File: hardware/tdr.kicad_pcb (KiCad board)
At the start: 4 copper layers, 98.8 x 47 mm, 238 parts, among them J201 Conn_02x01, J202 Conn_Coaxial, J203 Conn_Coaxial, J204 Conn_Coaxial, J205 Conn_Coaxial, J207 Conn_Coaxial, J208 Conn_Coaxial, J209 Conn_Coaxial, J210 Barrel_Jack_Switch, J801 Conn_02x06_Counter_Clockwise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

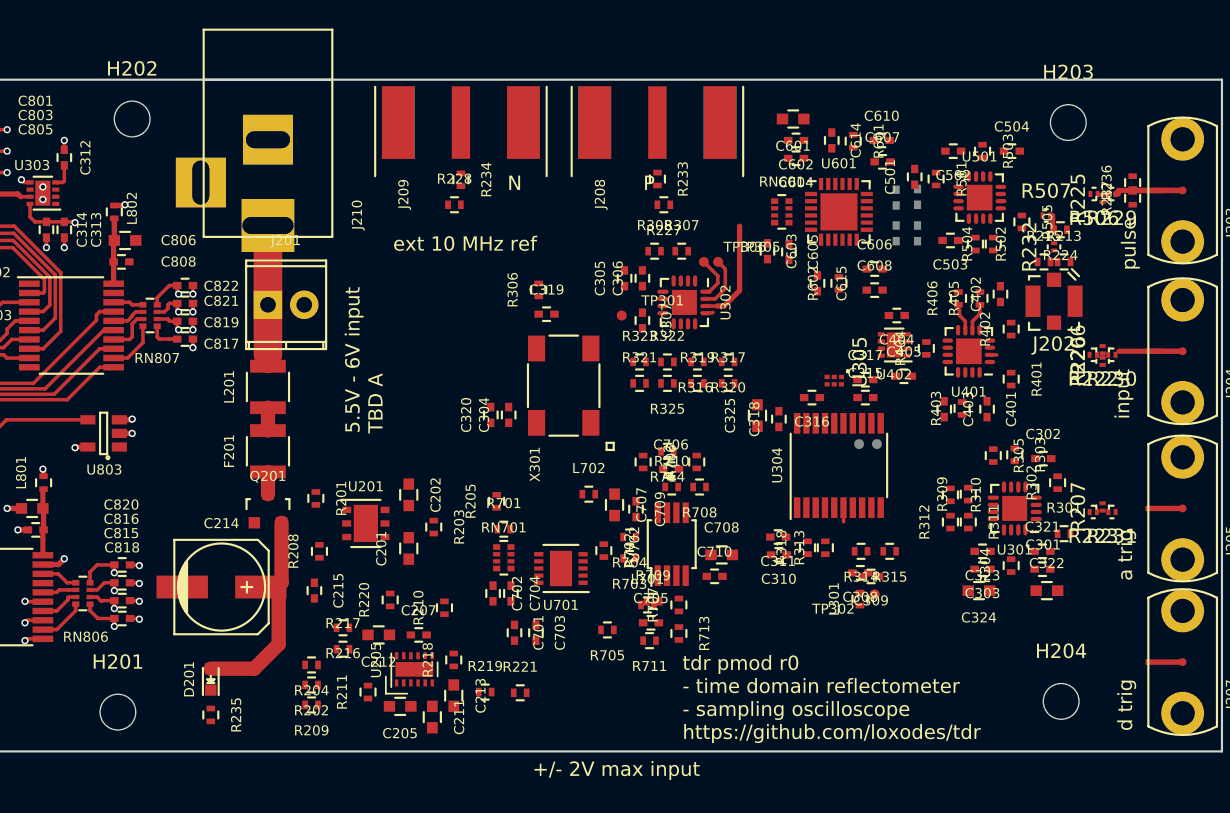
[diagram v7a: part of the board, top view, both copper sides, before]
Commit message: layout of low speed analog and power sections
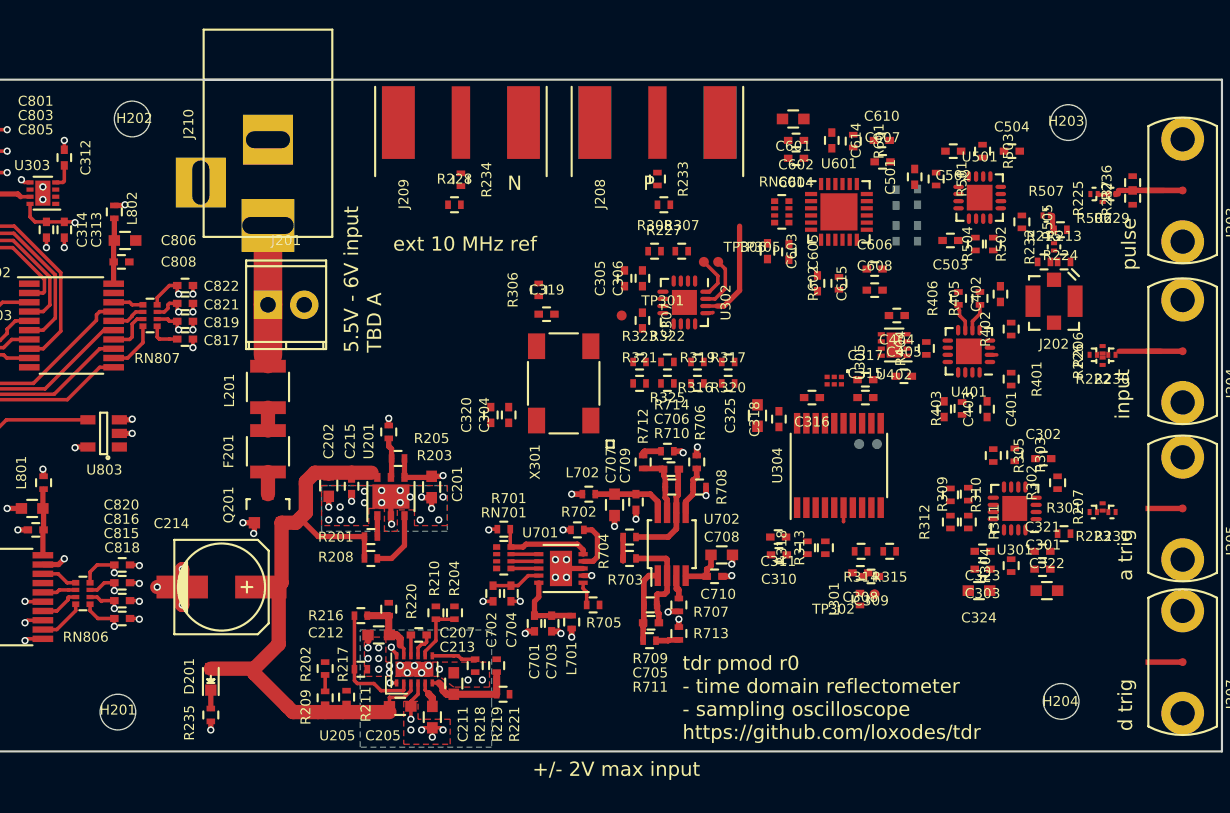
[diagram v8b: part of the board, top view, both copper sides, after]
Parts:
- moved R204 10.6 mm to (135.8, 95.8), turned to 90 degrees
- moved R205 8.97 mm to (131.2, 83.2), turned to 270 degrees
- moved C215 7.75 mm to (128.6, 87.0)
- moved C202 5.64 mm to (127.0, 86.9), turned to 90 degrees
- moved L701 5.43 mm to (144.0, 96.5), turned to 90 degrees
- moved R203 5.41 mm to (131.8, 85.0), turned to 0 degrees
- moved R201 4.69 mm to (130.0, 90.5), turned to 0 degrees
- moved C201 4.59 mm to (134.2, 87.0)
- moved R208 3.63 mm to (129.9, 92.0), turned to 0 degrees
- moved U201 2.57 mm to (131.4, 87.7), turned to 90 degrees
- moved R702 2.35 mm to (144.4, 90.0), turned to 0 degrees
- moved R705 2.02 mm to (145.5, 95.2)
- moved R219 2.02 mm to (138.8, 99.5), turned to 270 degrees
- moved R217 1.88 mm to (129.2, 99.8)
- moved R218 1.55 mm to (137.2, 99.5)
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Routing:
- net VPP: track 15.2 -> 47.6 mm
- net GND: track 22.9 -> 52.1 mm, vias 30 -> 94
- net Net-(R216-Pad2): track 0.00 -> 8.81 mm
- net Net-(C706-Pad2): track 0.00 -> 7.31 mm
- net Net-(C705-Pad2): track 0.00 -> 7.29 mm
- net Net-(R701-Pad2): track 0.00 -> 6.87 mm
- net Net-(C213-Pad2): track 0.00 -> 6.52 mm
- net Net-(C707-Pad1): track 0.00 -> 5.37 mm
- net Net-(C705-Pad1): track 0.00 -> 5.34 mm
- net /sheet5C262FB0/DAC_VREF: track 0.00 -> 5.29 mm
- net Net-(C212-Pad1): track 0.00 -> 5.04 mm
- net Net-(C701-Pad1): track 0.00 -> 5.02 mm
- net Net-(C706-Pad1): track 0.00 -> 4.58 mm
- net /PGOOD_3V3: track 0.90 -> 5.27 mm
- net Net-(R204-Pad1): track 0.00 -> 4.17 mm
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- added copper zone on B.Cu, net GND
- added copper zone on F.Cu, net GND
